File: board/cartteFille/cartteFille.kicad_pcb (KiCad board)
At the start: 2 copper layers, 60 x 100 mm, 65 parts, among them U1 LM358, U20 MCP23018-E/SS, U21-2 SN74LVC2G14DBVTG4, U23-4 SN74LVC2G14DBVTG4, U25-6 SN74LVC2G14DBVTG4, U27-8 SN74LVC2G14DBVTG4

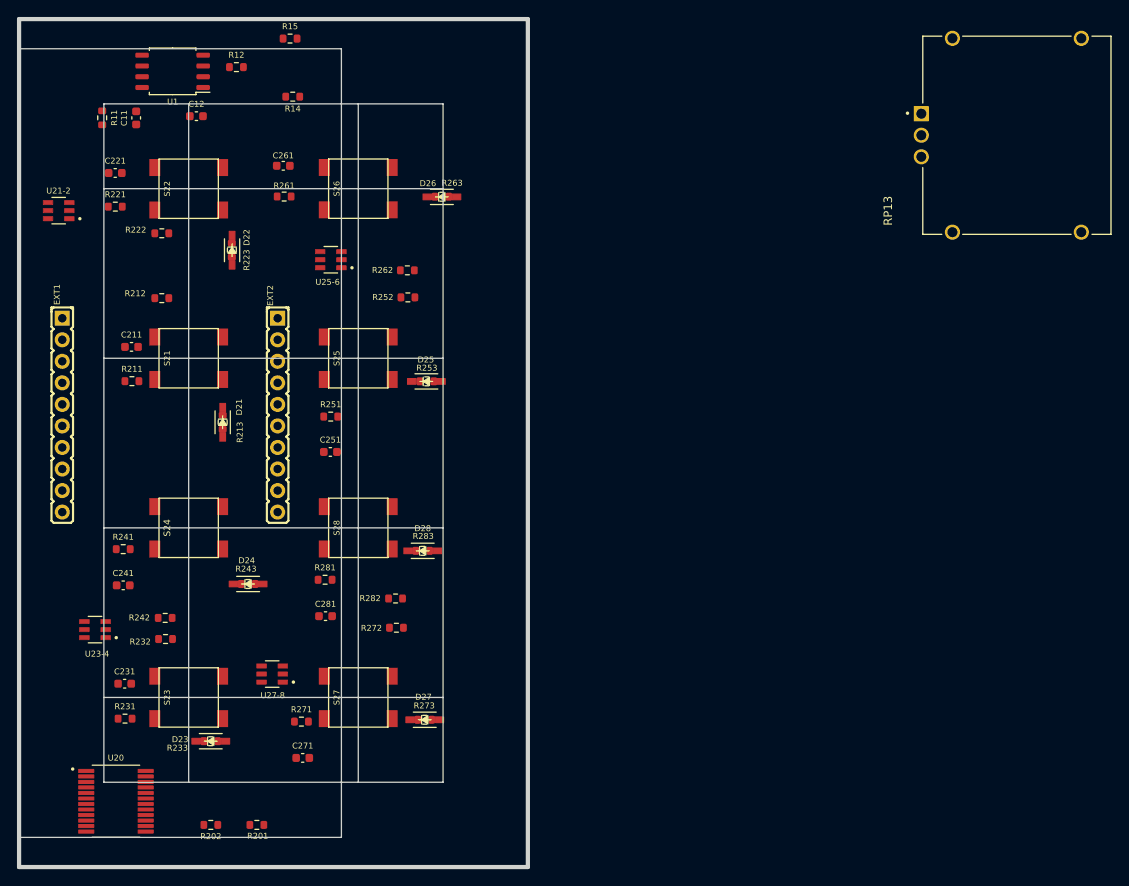
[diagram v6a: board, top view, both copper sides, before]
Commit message: pcb presque final
Les trous de montages doivent être réajuster
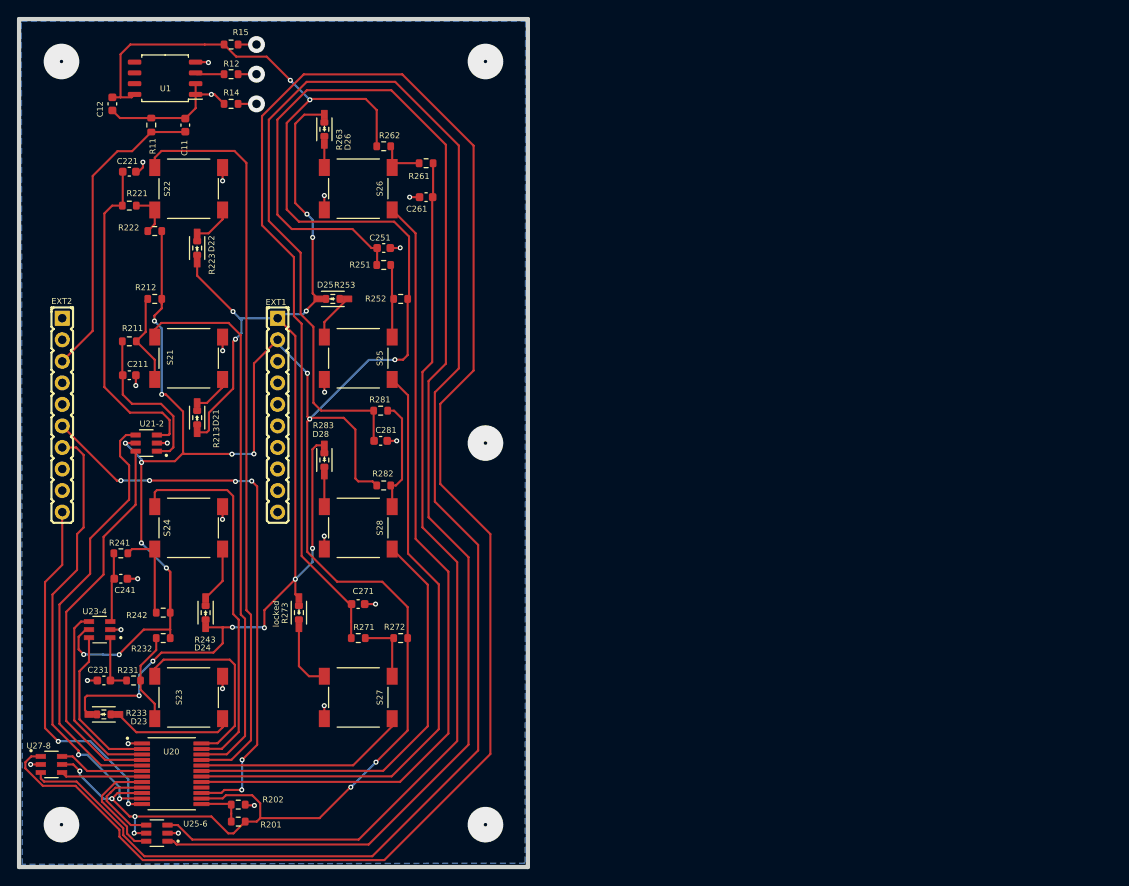
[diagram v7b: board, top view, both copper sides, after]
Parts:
- removed RP13: PCW1J-R24-BAB103L, PCW1J-R24-BAB103L:TRIM_PCW1J-R24-BAB103L
- D25: value NSI45020T1G -> NSI 45020T1G
- R11, R231, R281: value 10KOhm -> 10K
- R232, R272: value 1KOhm -> 1K
- U20: value MCP23018-E/SS -> MCP23018
- U21-2, U23-4, U25-6, U27-8: value SN74LVC2G14DBVTG4 -> SN74
- moved U25-6 70.7 mm to (16.2, 96.0)
- moved U21-2 29.3 mm to (15.0, 50.0)
- moved U27-8 28.1 mm to (3.81, 87.9), turned to 0 degrees
- moved EXT1 25.4 mm to (30.5, 46.7)
- moved EXT2 25.4 mm to (5.09, 46.7)
- moved C251 24.9 mm to (43.0, 27.0)
- moved C281 21.7 mm to (42.6, 49.7)
- moved R281 21.0 mm to (42.6, 46.2)
- moved R273 19.5 mm to (33.0, 70.0), turned to 90 degrees
- moved locked 19.5 mm to (33.0, 70.0), turned to 90 degrees
- moved C271 19.3 mm to (40.0, 69.0)
- moved R251 18.9 mm to (43.0, 29.0)
- moved C261 17.2 mm to (48.0, 21.0), turned to 180 degrees
- moved R261 17.2 mm to (48.0, 17.0), turned to 180 degrees
- moved D26 16.0 mm to (36.0, 13.0), turned to 90 degrees
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- renumbered D27 to locked
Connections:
- S21 pad K: /U20GPA4-S21LED -> /U20GPA5-S21LED
- S22 pad K: /U20GPA5-S22LED -> /U20GPA4-S22LED
- S23 pad K: /U20GPA6-S23LED -> /U20GPA7-S23LED
- S24 pad K: /U20GPA7-S24LED -> /U20GPA6-S24LED
- S25 pad K: /U20GPA0-S25LED -> /U20GPA1-S25LED
- S26 pad K: /U20GPA1-S26LED -> /U20GPA0-S26LED
- S27 pad K: /U20GPA2-S27LED -> /U20GPA3-S27LED
- S28 pad K: /U20GPA3-S28LED -> /U20GPA2-S28LED
- U20 pad 14: /GPIO3-U20RESET -> +3V3
- U20 pad 17: /U20GPA0-S25LED -> /U20GPA0-S26LED
- U20 pad 18: /U20GPA1-S26LED -> /U20GPA1-S25LED
- U20 pad 19: /U20GPA2-S27LED -> /U20GPA2-S28LED
- U20 pad 2: /U20GPB0-U256S25 -> /U20GPB0-U234S23
- U20 pad 20: /U20GPA3-S28LED -> /U20GPA3-S27LED
- U20 pad 21: /U20GPA4-S21LED -> /U20GPA4-S22LED
- U20 pad 22: /U20GPA5-S22LED -> /U20GPA5-S21LED
- U20 pad 23: /U20GPA6-S23LED -> /U20GPA6-S24LED
- U20 pad 24: /U20GPA7-S24LED -> /U20GPA7-S23LED
- U20 pad 3: /U20GPB1-U256S26 -> /U20GPB1-U234S24
- U20 pad 4: /U20GPB2-U278S27 -> /U20GPB2-U212S21
- U20 pad 5: /U20GPB3-U278S28 -> /U20GPB3-U212S22
- U20 pad 6: /U20GPB4-U212S21 -> /U20GPB4-U278S27
- U20 pad 7: /U20GPB5-U212S22 -> /U20GPB5-U278S28
- U20 pad 8: /U20GPB6-U234S23 -> /U20GPB6-U256S25
- U20 pad 9: /U20GPB7-U234S24 -> /U20GPB7-U256S26
- U21-2 pad 4: /U20GPB5-U212S22 -> /U20GPB3-U212S22
- U21-2 pad 6: /U20GPB4-U212S21 -> /U20GPB2-U212S21
- U23-4 pad 4: /U20GPB7-U234S24 -> /U20GPB1-U234S24
- U23-4 pad 6: /U20GPB6-U234S23 -> /U20GPB0-U234S23
- U25-6 pad 4: /U20GPB1-U256S26 -> /U20GPB7-U256S26
- U25-6 pad 6: /U20GPB0-U256S25 -> /U20GPB6-U256S25
- U27-8 pad 4: /U20GPB3-U278S28 -> /U20GPB5-U278S28
- U27-8 pad 6: /U20GPB2-U278S27 -> /U20GPB4-U278S27
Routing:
- net +3V3: track 0.00 -> 344.8 mm, vias 0 -> 21
- net Net-(C271-Pad1): track 0.00 -> 240.2 mm
- net Net-(C281-Pad1): track 0.00 -> 210.4 mm
- net Net-(C251-Pad1): track 0.00 -> 164.7 mm
- net +5V: track 0.00 -> 155.9 mm, vias 0 -> 11
- net Net-(C261-Pad1): track 0.00 -> 110.0 mm
- net /U20GPA0-S26LED: track 0.00 -> 96.0 mm
- net /U20GPA4-S22LED: track 0.00 -> 88.0 mm
- net /U20GPA1-S25LED: track 0.00 -> 73.8 mm
- net /GPIO32-INTB: track 0.00 -> 67.4 mm, vias 0 -> 6
- net /U20GPA5-S21LED: track 0.00 -> 65.5 mm
- net /U20GPA2-S28LED: track 0.00 -> 51.5 mm
- net /I2C_SCL: track 0.00 -> 51.5 mm, vias 0 -> 2
- net /U20GPB3-U212S22: track 0.00 -> 51.1 mm
- net GND: track 0.00 -> 49.1 mm, vias 0 -> 24
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- added copper zone on B.Cu, net GND
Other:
- outline, holes or cut-outs redrawn

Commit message: final_v1.0
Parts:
- added 1M4: MountingHole_4.3mm_M4_ISO14580, MountingHole:MountingHole_4.3mm_M4_ISO14580, F.Cu at (5.00, 5.00)
- added 2M4: MountingHole_4.3mm_M4_ISO14580, MountingHole:MountingHole_4.3mm_M4_ISO14580, F.Cu at (5.00, 95.0)
- added 3M4: MountingHole_4.3mm_M4_ISO14580, MountingHole:MountingHole_4.3mm_M4_ISO14580, F.Cu at (55.0, 95.0)
- added 4M4: MountingHole_4.3mm_M4_ISO14580, MountingHole:MountingHole_4.3mm_M4_ISO14580, F.Cu at (55.0, 50.0)
- added 5M4: MountingHole_4.3mm_M4_ISO14580, MountingHole:MountingHole_4.3mm_M4_ISO14580, F.Cu at (55.0, 5.00)
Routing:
- net (no net): vias 5 -> 0
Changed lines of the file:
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@@
     )
   )
+  (footprint "MountingHole:MountingHole_4.3mm_M4_ISO14580" (layer "F.Cu")
+    (at 5 95)
+    (descr "Mounting Hole 4.3mm, no annular, M4, ISO14580")
+    (tags "mounting hole 4.3mm no annular m4 iso14580")
+    (clearance 1.5)
+    (attr exclude_from_pos_files exclude_from_bom)
+    (fp_text reference "2M4" (at 4.43 3.28) (layer "F.SilkS")
+      (effects (font (size 1 1) (thickness 0.15)))
+    )
+    (fp_text value "MountingHole_4.3mm_M4_ISO14580" (at 0 4.5) (layer "F.Fab") hide
+      (effects (font (size 1 1) (thickness 0.15)))
+    )
+    (fp_text user "${REFERENCE}" (at 0 0) (layer "F.Fab") hide
+      (effects (font (size 1 1) (thickness 0.15)))
+    )
+    (fp_circle (center 0 0) (end 3.5 0) (layer "Cmts.User") (width 0.15) (fill none))
+    (fp_circle (center 0 0) (end 3.75 0) (layer "F.CrtYd") (width 0.05) (fill none))
+    (pad "" np_thru_hole circle (at 0 0) (size 4.3 4.3) (drill 4.3) (layers *.Cu *.Mask))
+  )
   (footprint "3006:3006.2100" locked (layer "F.Cu")
     (at 20 20.01 90)
@@
       (net 54 "/U20GPB0-U234S23") (pinfunction "1Y") (pintype "output"))
   )
+  (footprint "MountingHole:MountingHole_4.3mm_M4_ISO14580" (layer "F.Cu")
+    (at 55 95)
+    (descr "Mounting Hole 4.3mm, no annular, M4, ISO14580")
+    (tags "mounting hole 4.3mm no annular m4 iso14580")
+    (clearance 1.5)
+    (attr exclude_from_pos_files exclude_from_bom)
+    (fp_text reference "3M4" (at 2.19 -5.17) (layer "F.SilkS")
+      (effects (font (size 1 1) (thickness 0.15)))
+    )
+    (fp_text value "MountingHole_4.3mm_M4_ISO14580" (at 0 4.5) (layer "F.Fab") hide
+      (effects (font (size 1 1) (thickness 0.15)))
+    )
+    (fp_text user "${REFERENCE}" (at 0 0) (layer "F.Fab") hide
+      (effects (font (size 1 1) (thickness 0.15)))
+    )
+    (fp_circle (center 0 0) (end 3.5 0) (layer "Cmts.User") (width 0.15) (fill none))
+    (fp_circle (center 0 0) (end 3.75 0) (layer "F.CrtYd") (width 0.05) (fill none))
+    (pad "" np_thru_hole circle (at 0 0) (size 4.3 4.3) (drill 4.3) (layers *.Cu *.Mask))
+  )
   (footprint "Resistor_SMD:R_0603_1608Metric" (layer "F.Cu")
     (at 25 6.5 180)
@@
       (net 13 "+5V") (pintype "passive"))
   )
+  (footprint "MountingHole:MountingHole_4.3mm_M4_ISO14580" (layer "F.Cu")
+    (at 55 50)
+    (descr "Mounting Hole 4.3mm, no annular, M4, ISO14580")
+    (tags "mounting hole 4.3mm no annular m4 iso14580")
+    (clearance 1.5)
+    (attr exclude_from_pos_files exclude_from_bom)
+    (fp_text reference "4M4" (at 0.06 4.94) (layer "F.SilkS")
+      (effects (font (size 1 1) (thickness 0.15)))
+    )
+    (fp_text value "MountingHole_4.3mm_M4_ISO14580" (at 0 4.5) (layer "F.Fab") hide
+      (effects (font (size 1 1) (thickness 0.15)))
+    )
+    (fp_text user "${REFERENCE}" (at 0 0) (layer "F.Fab") hide
+      (effects (font (size 1 1) (thickness 0.15)))
+    )
+    (fp_circle (center 0 0) (end 3.5 0) (layer "Cmts.User") (width 0.15) (fill none))
+    (fp_circle (center 0 0) (end 3.75 0) (layer "F.CrtYd") (width 0.05) (fill none))
+    (pad "" np_thru_hole circle (at 0 0) (size 4.3 4.3) (drill 4.3) (layers *.Cu *.Mask))
+  )
   (footprint "3006:3006.2100" locked (layer "F.Cu")
     (at 20 80 90)
@@
       (net 48 "/U20GPA7-S23LED") (pintype "bidirectional"))
   )
+  (footprint "MountingHole:MountingHole_4.3mm_M4_ISO14580" (layer "F.Cu")
+    (at 55 5)
+    (descr "Mounting Hole 4.3mm, no annular, M4, ISO14580")
+    (tags "mounting hole 4.3mm no annular m4 iso14580")
+    (clearance 1.5)
+    (attr exclude_from_pos_files exclude_from_bom)
+    (fp_text reference "5M4" (at 0.06 4.94) (layer "F.SilkS")
+      (effects (font (size 1 1) (thickness 0.15)))
+    )
+    (fp_text value "MountingHole_4.3mm_M4_ISO14580" (at 0 4.5) (layer "F.Fab") hide
+      (effects (font (size 1 1) (thickness 0.15)))
+    )
+    (fp_text user "${REFERENCE}" (at 0 0) (layer "F.Fab") hide
+      (effects (font (size 1 1) (thickness 0.15)))
+    )
+    (fp_circle (center 0 0) (end 3.5 0) (layer "Cmts.User") (width 0.15) (fill none))
+    (fp_circle (center 0 0) (end 3.75 0) (layer "F.CrtYd") (width 0.05) (fill none))
+    (pad "" np_thru_hole circle (at 0 0) (size 4.3 4.3) (drill 4.3) (layers *.Cu *.Mask))
+  )
   (footprint "Resistor_SMD:R_0603_1608Metric" (layer "F.Cu")
     (at 43 55 180)
@@
     (property "Sheetname" "ButtonS27-S28_Sheet")
     (attr through_hole)
-    (fp_text reference "U27-8" (at -1.505 -2.2) (layer "F.SilkS")
+    (fp_text reference "U27-8" (at -1.525 -2.32) (layer "F.SilkS")
       (effects (font (size 0.7 0.7) (thickness 0.15)))
     )
@@
     )
   )
+  (footprint "MountingHole:MountingHole_4.3mm_M4_ISO14580" (layer "F.Cu")
+    (at 5 5)
+    (descr "Mounting Hole 4.3mm, no annular, M4, ISO14580")
+    (tags "mounting hole 4.3mm no annular m4 iso14580")
+    (clearance 1.5)
+    (attr exclude_from_pos_files exclude_from_bom)
+    (fp_text reference "1M4" (at 0.06 4.94) (layer "F.SilkS")
+      (effects (font (size 1 1) (thickness 0.15)))
+    )
+    (fp_text value "MountingHole_4.3mm_M4_ISO14580" (at 0 4.5) (layer "F.Fab") hide
+      (effects (font (size 1 1) (thickness 0.15)))
+    )
+    (fp_text user "${REFERENCE}" (at 0 0) (layer "F.Fab") hide
+      (effects (font (size 1 1) (thickness 0.15)))
+    )
+    (fp_circle (center 0 0) (end 3.5 0) (layer "Cmts.User") (width 0.15) (fill none))
+    (fp_circle (center 0 0) (end 3.75 0) (layer "F.CrtYd") (width 0.05) (fill none))
+    (pad "" np_thru_hole circle (at 0 0) (size 4.3 4.3) (drill 4.3) (layers *.Cu *.Mask))
+  )
   (gr_rect locked (start 0 0) (end 60 100) (layer "Edge.Cuts") (width 0.5) (fill none))
-  (via (at 55 95) (size 4.2) (drill 0.4) (layers "F.Cu" "B.Cu") (free) (net 0))
-  (via (at 5 5) (size 4.2) (drill 0.4) (layers "F.Cu" "B.Cu") (free) (net 0))
-  (via (at 55 5) (size 4.2) (drill 0.4) (layers "F.Cu" "B.Cu") (free) (net 0))
-  (via (at 55 50) (size 4.2) (drill 0.4) (layers "F.Cu" "B.Cu") (free) (net 0))
-  (via (at 5 95) (size 4.2) (drill 0.4) (layers "F.Cu" "B.Cu") (free) (net 0))
   (segment (start 15.59 13.32) (end 19.56 13.32) (width 0.25) (layer "F.Cu") (net 1))
   (segment (start 8.68 36.772) (end 5.092 40.36) (width 0.25) (layer "F.Cu") (net 1))
@@
   (segment (start 27.725 92.72) (end 26.75 92.72) (width 0.25) (layer "F.Cu") (net 2))
   (segment (start 20.82 7.615) (end 20.82 8.885) (width 0.25) (layer "F.Cu") (net 2))
-  (segment (start 14.48 85.41) (end 14.495 85.425) (width 0.25) (layer "F.Cu") (net 2))
   (segment (start 35.99 60.97) (end 36 60.98) (width 0.25) (layer "F.Cu") (net 2))
   (segment (start 43.775 27) (end 44.92 27) (width 0.25) (layer "F.Cu") (net 2))
@@
   (segment (start 4.62 85.18) (end 4.65 85.15) (width 0.25) (layer "B.Cu") (net 35))
   (segment (start 12.88 92.50989) (end 12.9 92.52989) (width 0.25) (layer "B.Cu") (net 35))
-  (segment (start 28.75 10) (end 28.8 9.95) (width 0.25) (layer "F.Cu") (net 37))
   (segment (start 25.825 10) (end 28 10) (width 0.25) (layer "F.Cu") (net 37))
   (via (at 28 10) (size 2) (drill 1) (layers "F.Cu" "B.Cu") (net 37))
@@
   (segment (start 12.611307 49.05) (end 13.745 49.05) (width 0.25) (layer "F.Cu") (net 57))
   (segment (start 14.495 88.025) (end 14.475 88.005) (width 0.25) (layer "F.Cu") (net 57))
-  (segment (start 14.495 88.675) (end 14.475 88.655) (width 0.25) (layer "F.Cu") (net 58))
   (segment (start 8.045 88.675) (end 6.32 86.95) (width 0.25) (layer "F.Cu") (net 58))
-  (segment (start 6.32 86.95) (end 5.07 86.95) (width 0.25) (layer "F.Cu") (net 58))
   (segment (start 14.495 88.675) (end 8.045 88.675) (width 0.25) (layer "F.Cu") (net 58))
+  (segment (start 6.32 86.95) (end 5.07 86.95) (width 0.25) (layer "F.Cu") (net 58))
   (segment (start 14.495 89.325) (end 5.545 89.325) (width 0.25) (layer "F.Cu") (net 59))
   (segment (start 5.545 89.325) (end 5.07 88.85) (width 0.25) (layer "F.Cu") (net 59))
